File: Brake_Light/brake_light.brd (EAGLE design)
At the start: 60.9 x 116.5 mm, 88 parts, among them IC1 LM556D, T2 2SC1307, X1 PWR

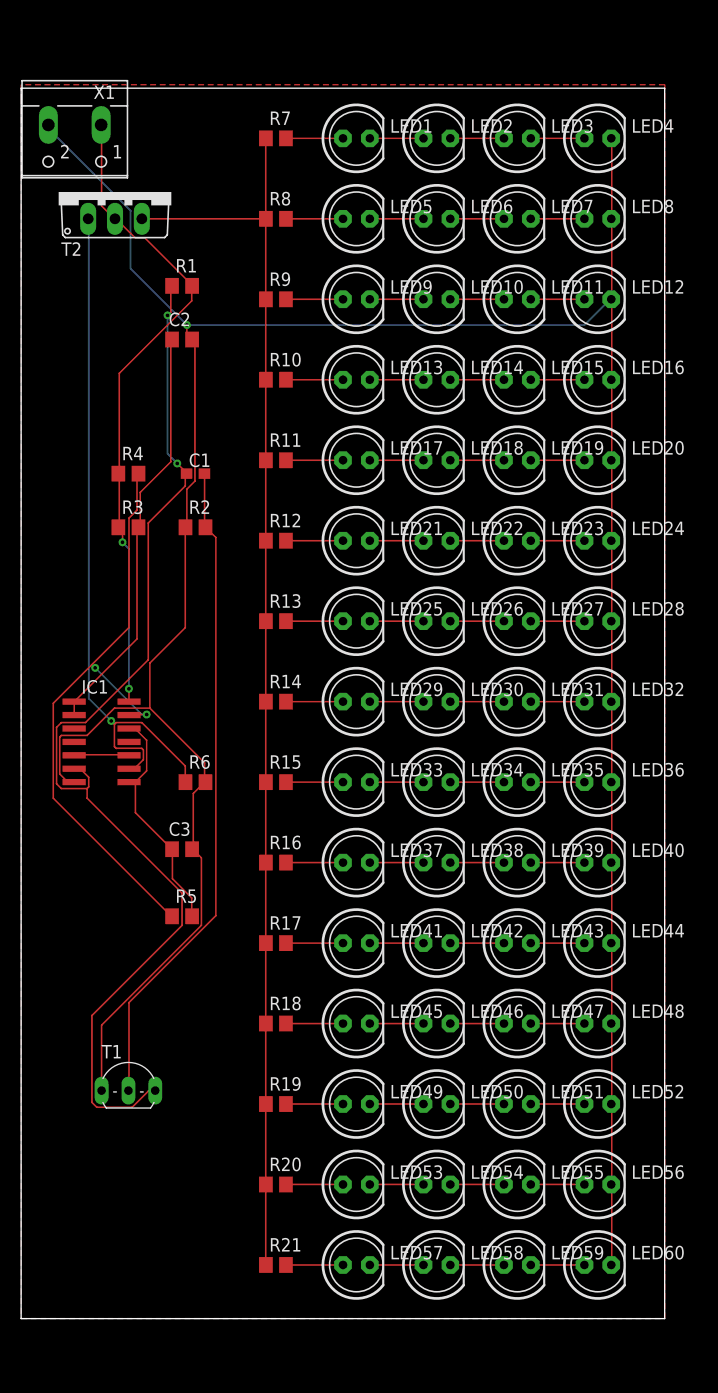
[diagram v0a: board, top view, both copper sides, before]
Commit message: Switched to a simpler design
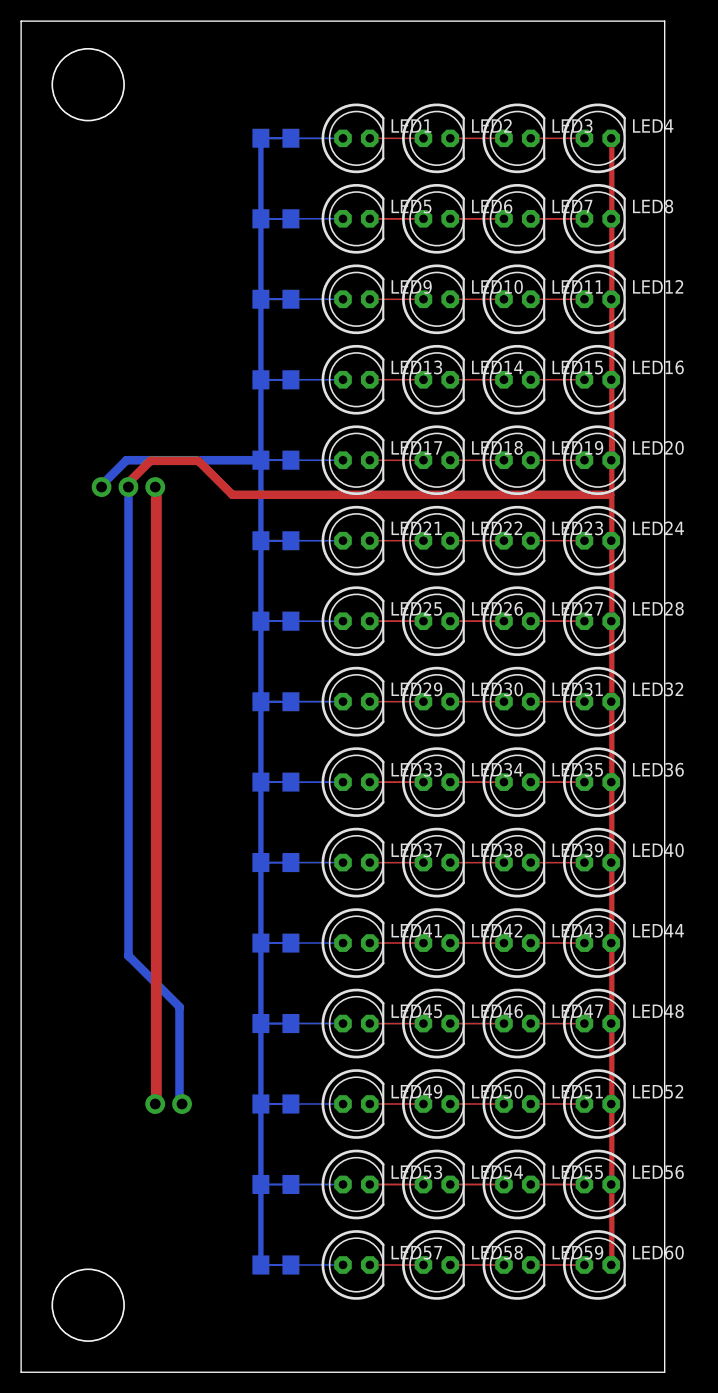
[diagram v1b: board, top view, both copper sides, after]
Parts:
- removed C1: .001uF, eagle-ltspice:C0603
- removed C2: 10uF, eagle-ltspice:C0805
- removed C3: 1uF, eagle-ltspice:C0805
- removed IC1: LM556D, linear:SO14
- removed R1, R2: 221k, eagle-ltspice:R0805
- removed R3, R4, R5: 100k, eagle-ltspice:R0805
- removed R6: 100, eagle-ltspice:R0805
- removed T1: (no value), transistor:TO92-EBC
- removed T2: 2SC1307, transistor:TO220AV
- removed X1: PWR, con-wago-500:W237-102
- added J1: (no value), SparkFun-Connectors:1X02
- added J2: TI LM78M05CT/NOPB, SparkFun-Connectors:1X03
- R10, R11, R12, R13, R14, R15, R16, R17, R18, R19, R20, R21, R7, R8: device eagle-ltspice:R0805 -> eagle-ltspice:R1206
- R9: value 50] -> 50; device eagle-ltspice:R0805 -> eagle-ltspice:R1206
- flipped R10 to the bottom
- flipped R11 to the bottom
- flipped R12 to the bottom
- flipped R13 to the bottom
- flipped R14 to the bottom
- flipped R15 to the bottom
- flipped R16 to the bottom
- flipped R17 to the bottom
- flipped R18 to the bottom
- flipped R19 to the bottom
- flipped R20 to the bottom
- flipped R21 to the bottom
- flipped R7 to the bottom
- flipped R8 to the bottom
- flipped R9 to the bottom
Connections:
- removed net N$1: C2.1, IC1.1, IC1.2, R3.2
- removed net N$2: IC1.10, IC1.5
- removed net N$3: C1.1, IC1.6, R1.1, T1.C
- removed net N$4: C1.2, R2.2, T1.B
- removed net N$6: C3.1, IC1.12, IC1.8, R5.2
- removed net N$7: IC1.13, R4.2, R5.1
- removed net N$8: IC1.9, R6.1, T2.1
- removed net N$9: R10.1, R11.1, R12.1, R13.1, R14.1, R15.1, R16.1, R17.1, R18.1, R19.1, R20.1, R21.1, R7.1, R8.1, R9.1, T2.3
- removed net VCC(5V): IC1.14, R1.2, R3.1, R4.1, T2.2, X1.1
- new net 12V: J1.2, J2.1
- new net 5V: J2.3, R10.1, R11.1, R12.1, R13.1, R14.1, R15.1, R16.1, R17.1, R18.1, R19.1, R20.1, R21.1, R7.1, R8.1, R9.1
- net GND: now also J1.1, J2.2; no longer C2.2, C3.2, IC1.7, R2.1, R6.2, T1.E, X1.2
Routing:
- net 5V: track 0.00 -> 165.7 mm, vias 0 -> 1
- net N$9: track 118.6 -> 0.00 mm
- net N$3: track 104.3 -> 0.00 mm, vias 2 -> 0
- net N$8: track 66.6 -> 0.00 mm, vias 1 -> 0
- net VCC(5V): track 64.5 -> 0.00 mm, vias 2 -> 0
- net N$4: track 62.3 -> 0.00 mm
- net N$7: track 58.8 -> 0.00 mm, vias 2 -> 0
- net 12V: track 0.00 -> 58.6 mm
- net GND: track 271.9 -> 218.6 mm
- net N$1: track 39.5 -> 0.00 mm
- net N$6: track 22.2 -> 0.00 mm
- net N$2: track 5.28 -> 0.00 mm
- net N$66: track 5.40 -> 7.77 mm
- net N$62: track 5.40 -> 7.77 mm
- net N$58: track 5.40 -> 7.77 mm
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- removed copper zone on layer 1, net GND
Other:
- board size 60.9 x 116.5 mm -> 60.9 x 127.9 mm
- board text added: "12V"
- board text added: "GND"
